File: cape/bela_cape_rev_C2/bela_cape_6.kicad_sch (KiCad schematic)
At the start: 49 parts, among them IC4 TL974, IC5 TL974, IC6 ES9080Q, J12 Conn_01x03, J13 Conn_01x03, J14 Conn_01x03, J15 Conn_01x03

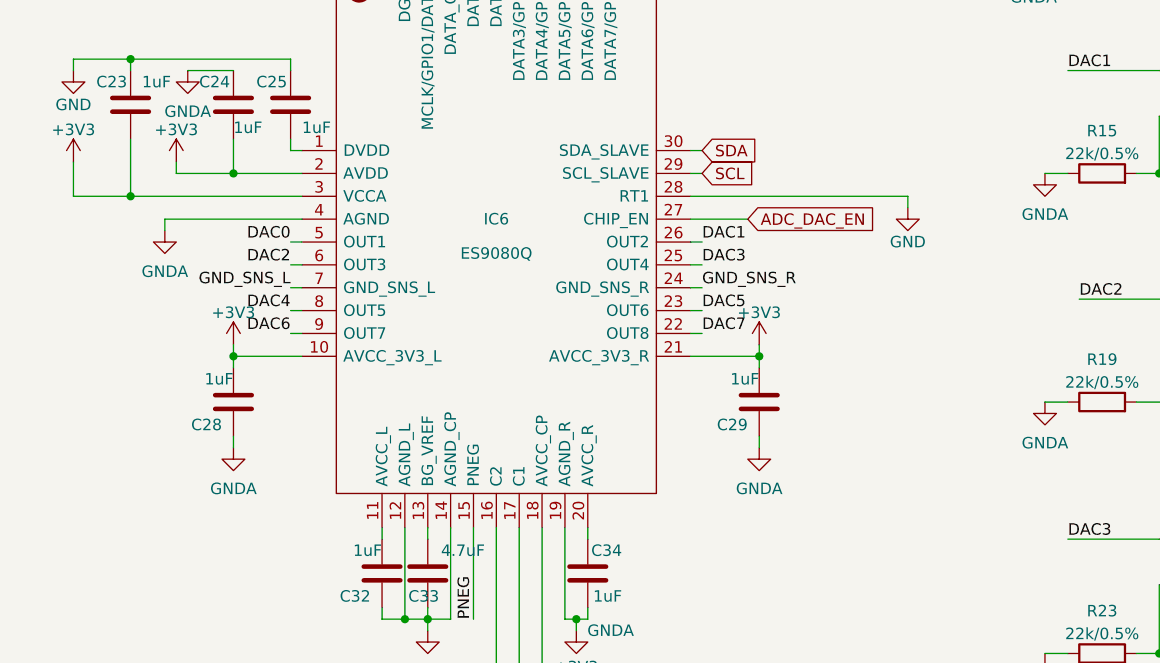
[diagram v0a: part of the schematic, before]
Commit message: Bela cape rev. C2
(cherry picked from commit 085b3700cd1d9a25c77092a8b59a7c103f45927b)
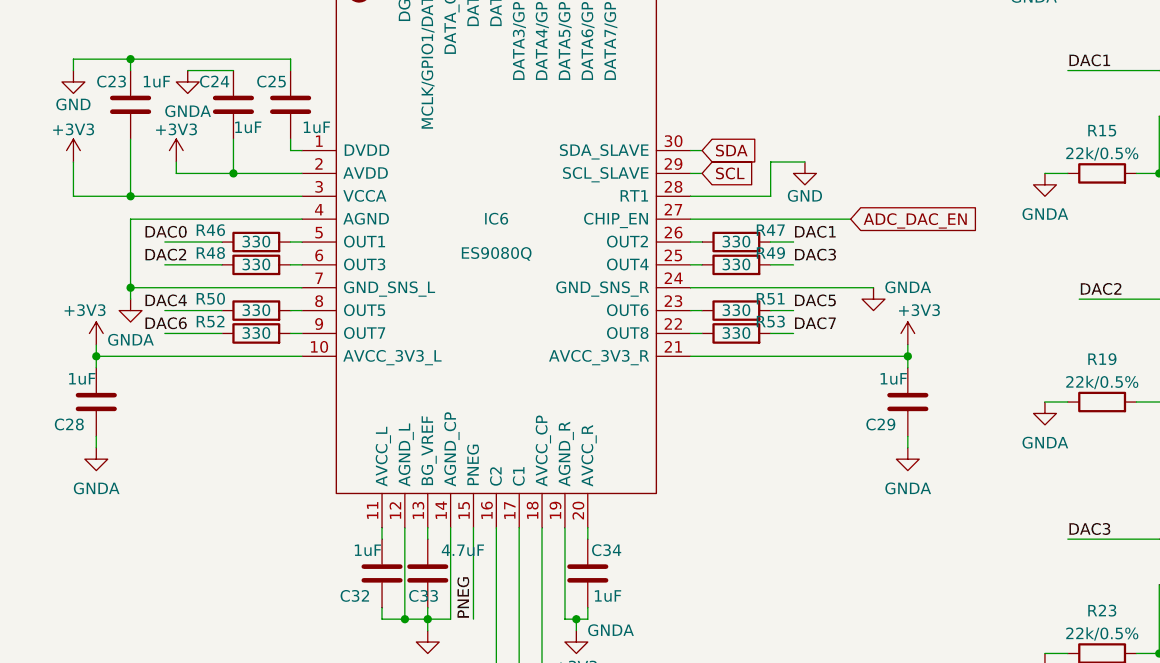
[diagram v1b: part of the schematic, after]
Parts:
- added R46, R47, R48, R49, R50, R51, R52, R53: 330, Resistor_SMD:R_0603_1608Metric, symbol Device:R
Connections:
- net GND_SNS_L is gone; now on net GNDA: IC6.7 (GND_SNS_L)
- net GND_SNS_R is gone; now on net GNDA: IC6.24 (GND_SNS_R)
- net DAC0: now also R46.1; no longer IC6.5 (OUT1)
- net DAC1: now also R47.2; no longer IC6.26 (OUT2)
- net DAC2: now also R48.1; no longer IC6.6 (OUT3)
- net DAC3: now also R49.2; no longer IC6.25 (OUT4)
- net DAC4: now also R50.1; no longer IC6.8 (OUT5)
- net DAC5: now also R51.2; no longer IC6.23 (OUT6)
- net DAC6: now also R52.1; no longer IC6.9 (OUT7)
- net DAC7: now also R53.2; no longer IC6.22 (OUT8)
- new net: IC6.22 (OUT8), R53.1
- new net: IC6.9 (OUT7), R52.2
- new net: IC6.23 (OUT6), R51.1
- new net: IC6.25 (OUT4), R49.1
- new net: IC6.26 (OUT2), R47.1
- new net: IC6.5 (OUT1), R46.2
- new net: IC6.6 (OUT3), R48.2
- new net: IC6.8 (OUT5), R50.2
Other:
- moved on the sheet: C28, C29
